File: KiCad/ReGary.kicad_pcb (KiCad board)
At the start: 4 copper layers, 38 x 38 mm, 39 parts, among them J1 Conn_01x02, U1 GW1N-UV1P5LQ100, U2 LM1117-3.3, U3 TPS73643DBV, U4 SN74CBT16210, U5 SN74CBT16210, U6 SN74CBT16210, U7 SN74CBT16210, U8 PLCC_84_plug, U9 PLCC_84_plug

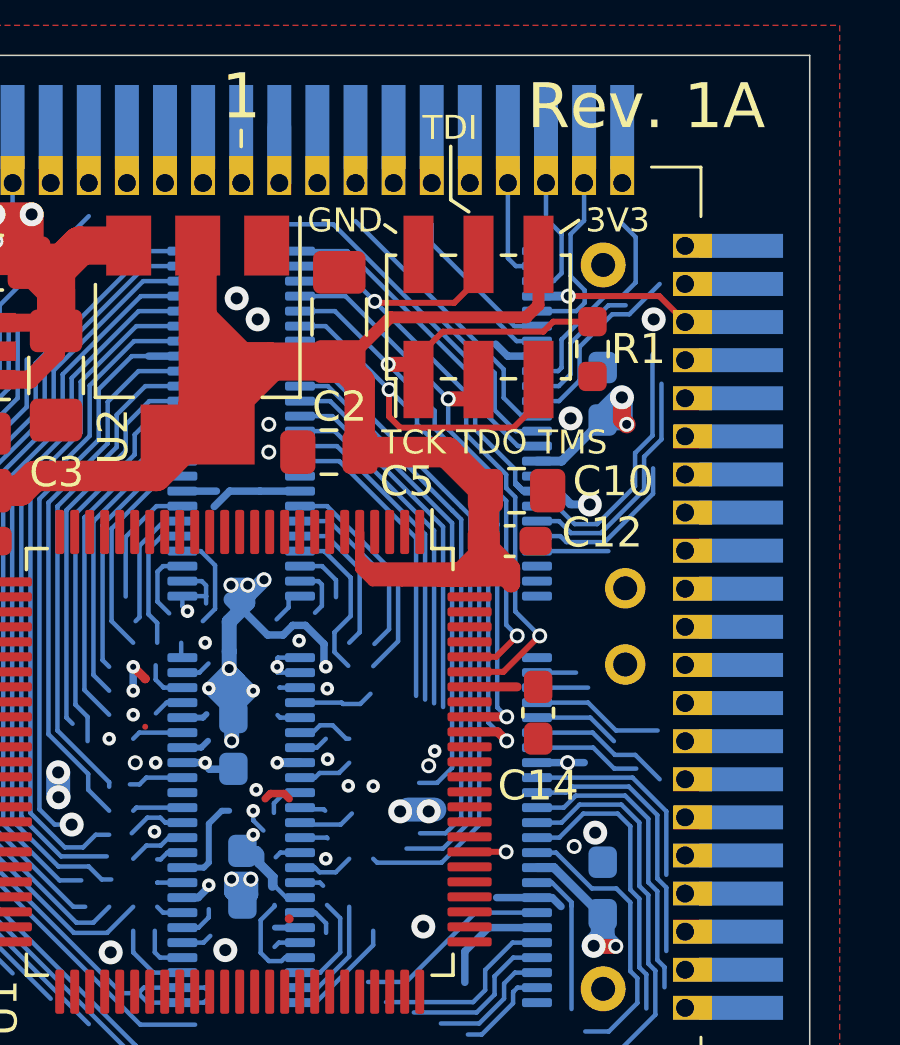
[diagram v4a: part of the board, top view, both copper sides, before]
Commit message: More signal to pin assignments and routing
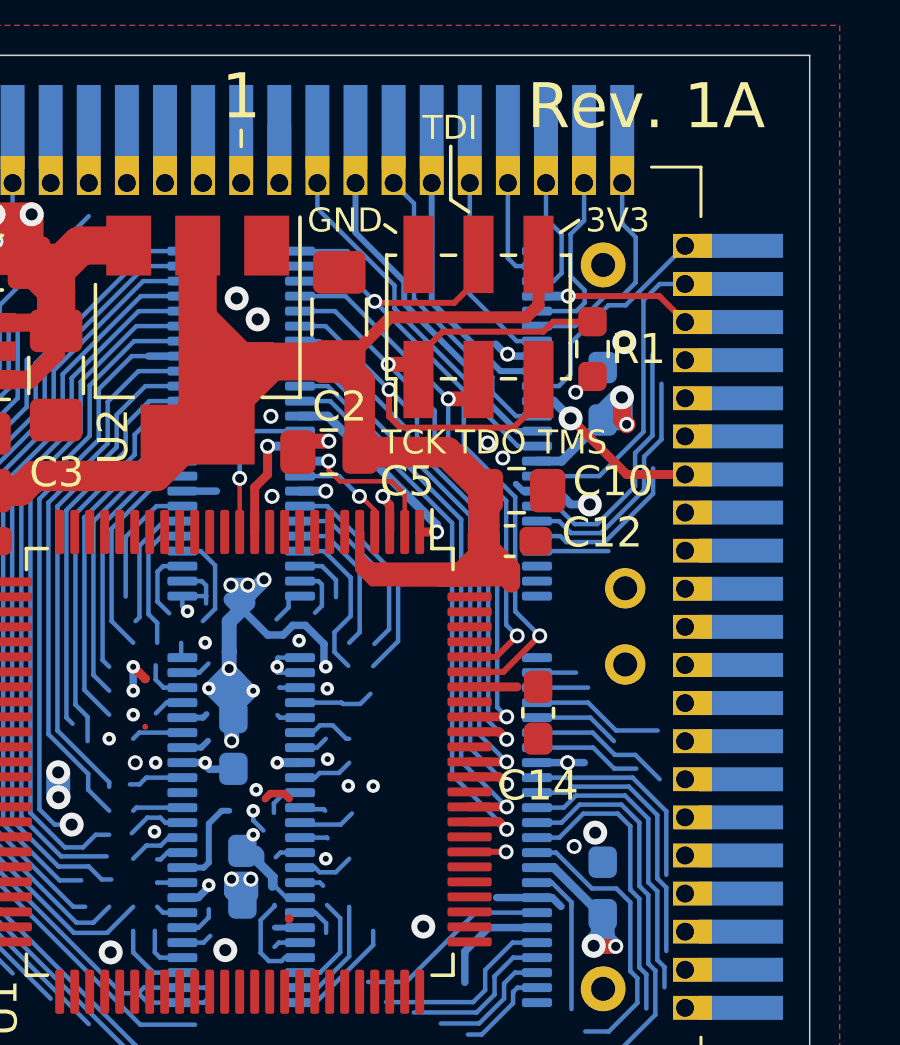
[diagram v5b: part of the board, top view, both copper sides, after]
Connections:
- net Net-(U1-Pad11) renamed /ReGary_FPGA/NC
- net Net-(U1-Pad20) renamed GCLKT_5
- net Net-(U1-Pad3) renamed GCLKT_7
- net Net-(U1-Pad34) renamed GCLKT_4
- net Net-(U1-Pad38) renamed GCLKT_3
- net Net-(U1-Pad63) renamed GCLKT_2
- U1 pad 1: Net-(U1-Pad1) -> C28M_FPGA
- U1 pad 12: Net-(U1-Pad12) -> XCLK_FPGA
- U1 pad 13: Net-(U1-Pad13) -> XCLKEN_FPGA
- U1 pad 2: Net-(U1-Pad2) -> BIGZ_FPGA
- U1 pad 4: Net-(U1-Pad4) -> STERM_FPGA
- U1 pad 84: Net-(U1-Pad84) -> DS_FPGA
- U1 pad 85: Net-(U1-Pad85) -> AGCLK_FPGA
- U1 pad 87: Net-(U1-Pad87) -> UUDS_FPGA
- U1 pad 88: Net-(U1-Pad88) -> C3_FPGA
- U4 pad 10: EBG0 -> DS
- U4 pad 11: EBG1 -> C28M
- U4 pad 12: BINT -> XCLKEN
- U4 pad 13: EDS1 -> XCLK
- U4 pad 14: FCS -> BIGZ
- U4 pad 16: GND -> STERM
- U4 pad 33: Net-(U4-Pad33) -> STERM_FPGA
- U4 pad 34: FCS_FPGA -> BIGZ_FPGA
- U4 pad 35: EDS1_FPGA -> XCLK_FPGA
- U4 pad 36: BINT_FPGA -> XCLKEN_FPGA
- U4 pad 37: EBG1_FPGA -> C28M_FPGA
- U4 pad 38: EBG0_FPGA -> DS_FPGA
- U4 pad 39: ABOE1_FPGA -> AGCLK_FPGA
- U4 pad 40: MS0_FPGA -> UUDS_FPGA
- U4 pad 42: EBR0_FPGA -> C3_FPGA
- U4 pad 6: EBR0 -> C3
- U4 pad 7: MS0 -> UUDS
- U4 pad 9: ABOE1 -> AGCLK
- U8 pad 43: Net-(U8-Pad43) -> CPUCLK
- U8 pad 44: Net-(U8-Pad44) -> KBCLK
- U8 pad 64: Net-(U8-Pad64) -> ECLK
- U8 pad 65: Net-(U8-Pad65) -> C1
- U8 pad 66: Net-(U8-Pad66) -> CDAC
- U8 pad 67: Net-(U8-Pad67) -> C7M
- U8 pad 68: Net-(U8-Pad68) -> C28M
- U8 pad 69: Net-(U8-Pad69) -> TEST
- U8 pad 70: Net-(U8-Pad70) -> CLK90
- U8 pad 71: Net-(U8-Pad71) -> D31
- U8 pad 73: Net-(U8-Pad73) -> STERM
- U8 pad 74: Net-(U8-Pad74) -> DS
- U8 pad 75: Net-(U8-Pad75) -> C3
- U8 pad 80: Net-(U8-Pad80) -> AGCLK
- U8 pad 81: Net-(U8-Pad81) -> XCLKEN
- U8 pad 82: Net-(U8-Pad82) -> XCLK
- U8 pad 83: Net-(U8-Pad83) -> BIGZ
- U9 pad 43: Net-(U9-Pad43) -> CPUCLK
- U9 pad 44: Net-(U9-Pad44) -> KBCLK
- U9 pad 64: Net-(U9-Pad64) -> ECLK
- U9 pad 65: Net-(U9-Pad65) -> C1
- U9 pad 66: Net-(U9-Pad66) -> CDAC
- U9 pad 67: Net-(U9-Pad67) -> C7M
- U9 pad 68: Net-(U9-Pad68) -> C28M
- U9 pad 69: Net-(U9-Pad69) -> TEST
- U9 pad 70: Net-(U9-Pad70) -> CLK90
- U9 pad 71: Net-(U9-Pad71) -> D31
- U9 pad 73: Net-(U9-Pad73) -> STERM
- U9 pad 74: Net-(U9-Pad74) -> DS
- U9 pad 75: Net-(U9-Pad75) -> C3
- U9 pad 80: Net-(U9-Pad80) -> AGCLK
- U9 pad 81: Net-(U9-Pad81) -> XCLKEN
- U9 pad 82: Net-(U9-Pad82) -> XCLK
- U9 pad 83: Net-(U9-Pad83) -> BIGZ
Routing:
- net MS0_FPGA: track 20.4 -> 0.00 mm
- net DS_FPGA: track 25.7 -> 44.8 mm, vias 0 -> 1
- net ABOE1_FPGA: track 18.7 -> 0.00 mm
- net AGCLK_FPGA: track 0.00 -> 18.7 mm, vias 0 -> 1
- net C3_FPGA: track 0.00 -> 18.5 mm, vias 0 -> 1
- net UUDS_FPGA: track 0.00 -> 18.5 mm, vias 0 -> 1
- net EBG0_FPGA: track 16.2 -> 0.00 mm
- net EBR0_FPGA: track 15.4 -> 0.00 mm
- net EBG1_FPGA: track 12.3 -> 0.00 mm
- net FCS: track 12.3 -> 0.00 mm
- net BIGZ: track 2.38 -> 14.6 mm
- net BINT_FPGA: track 11.6 -> 0.00 mm
- net XCLK: track 0.00 -> 11.2 mm
- net EDS1_FPGA: track 10.9 -> 0.00 mm
- net GND: track 124.4 -> 114.0 mm, vias 42 -> 44
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- removed copper zone on 4V3.Cu, net 3V3
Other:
- net class Default: via_dia 0.45 -> 0.5; via_drill 0.2 -> 0.3
- rule via_min_size: 0.45 -> 0.5

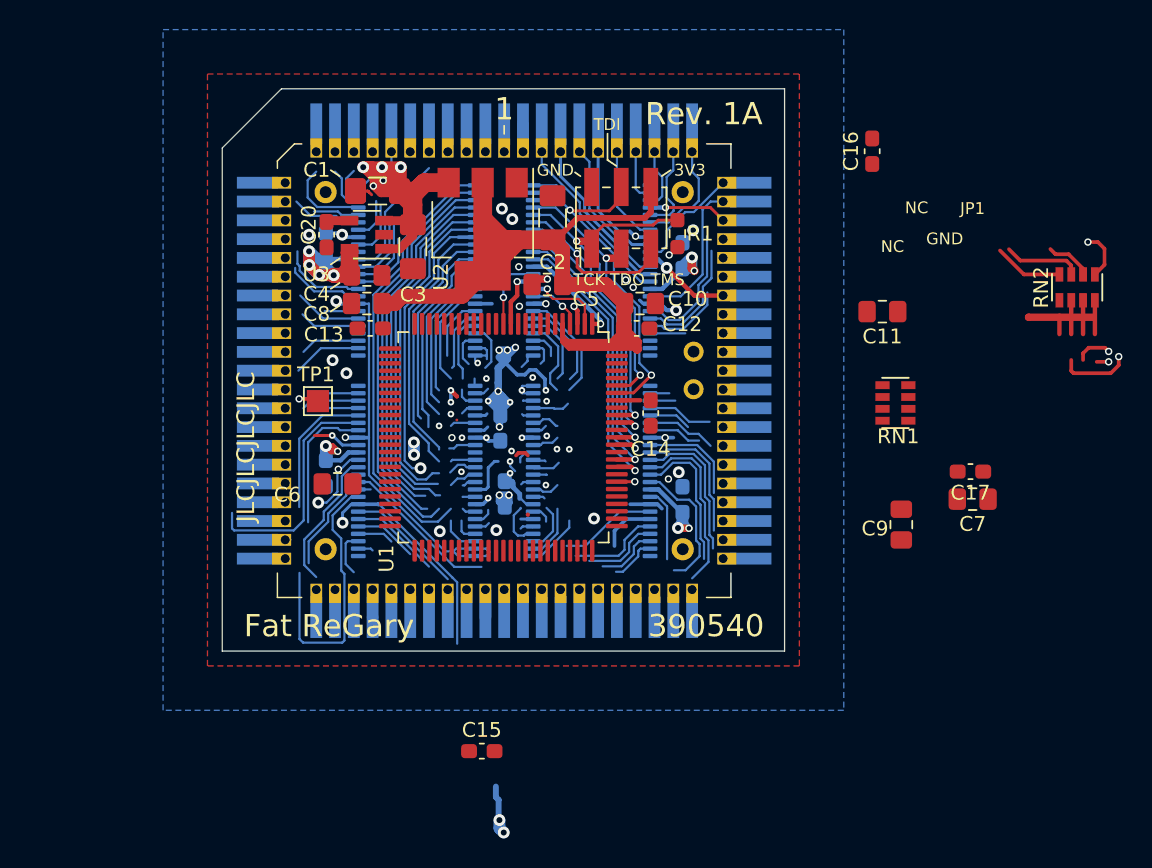
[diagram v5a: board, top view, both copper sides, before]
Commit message: More FPGA pin assignments and routing
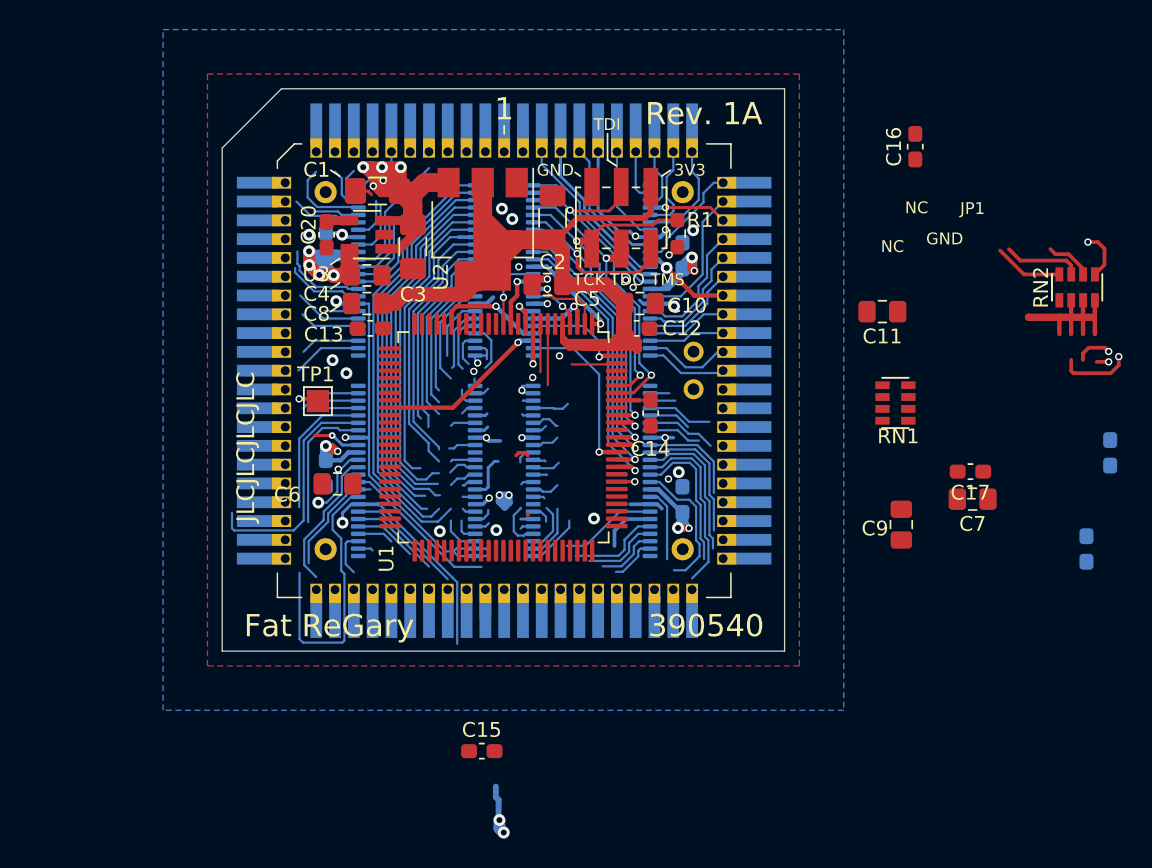
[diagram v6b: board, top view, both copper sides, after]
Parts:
- moved C19 41.2 mm to (185.4, 80.0)
- moved C18 39.5 mm to (183.8, 86.5)
- moved C16 2.93 mm to (172.2, 59.3)
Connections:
- U1 pad 10: Net-(U1-Pad10) -> D31_FPGA
- U1 pad 20: GCLKT_5 -> C7M_FPGA
- U1 pad 3: GCLKT_7 -> CLK90_FPGA
- U1 pad 34: GCLKT_4 -> CDAC_FPGA
- U1 pad 86: Net-(U1-Pad86) -> C1_FPGA
- U1 pad 9: Net-(U1-Pad9) -> ECLK_FPGA
- U1 pad 99: Net-(U1-Pad99) -> TEST_FPGA
- U4 pad 18: EBG2 -> D31
- U4 pad 19: EBG3 -> CLK90
- U4 pad 20: EBG4 -> TEST
- U4 pad 21: BIGZ -> C7M
- U4 pad 22: SLAVE0 -> CDAC
- U4 pad 23: SLAVE1 -> C1
- U4 pad 24: SLAVE2 -> ECLK
- U4 pad 25: SLAVE2_FPGA -> ECLK_FPGA
- U4 pad 26: SLAVE1_FPGA -> C1_FPGA
- U4 pad 27: SLAVE0_FPGA -> CDAC_FPGA
- U4 pad 28: BIGZ_FPGA -> C7M_FPGA
- U4 pad 29: EBG4_FPGA -> TEST_FPGA
- U4 pad 30: EBG3_FPGA -> CLK90_FPGA
- U4 pad 31: EBG2_FPGA -> D31_FPGA
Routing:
- net 3V3: track 121.3 -> 94.3 mm, vias 19 -> 4
- net C1_FPGA: track 0.00 -> 11.6 mm, vias 0 -> 1
- net CDAC_FPGA: track 3.11 -> 14.7 mm, vias 0 -> 1
- net TDO: track 10.3 -> 0.00 mm
- net D31: track 0.00 -> 8.68 mm
- net EBG2: track 8.67 -> 0.00 mm
- net EBG3: track 8.12 -> 0.01 mm
- net CLK90: track 3.76 -> 11.5 mm
- net EBG2_FPGA: track 7.56 -> 0.00 mm, vias 1 -> 0
- net C7M_FPGA: track 0.95 -> 8.20 mm, vias 0 -> 1
- net TEST_FPGA: track 0.00 -> 7.16 mm, vias 0 -> 1
- net GND: track 114.0 -> 106.9 mm, vias 44 -> 35
- net 4V3: track 41.8 -> 48.8 mm
- net TEST: track 0.00 -> 6.76 mm
- net TCK: track 11.4 -> 4.68 mm
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
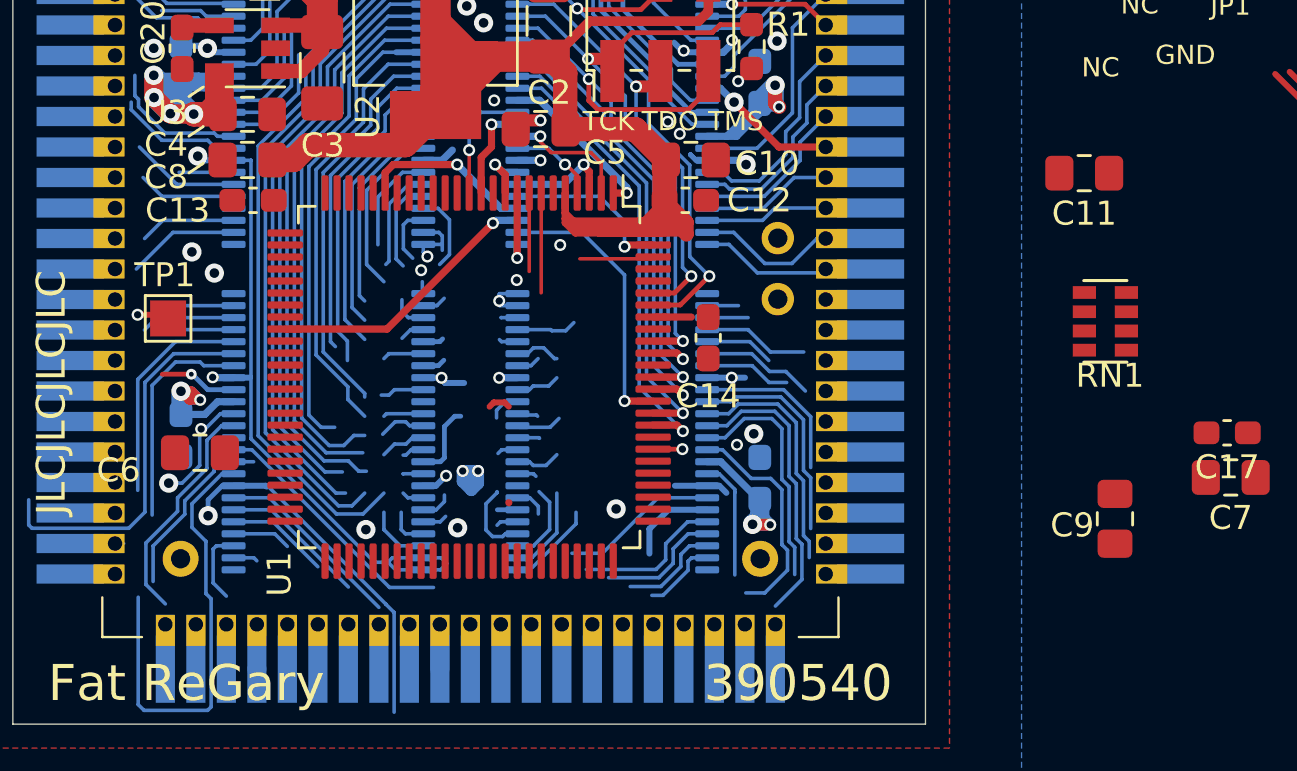
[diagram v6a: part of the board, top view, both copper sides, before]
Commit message: More signal to pin assignments and routing
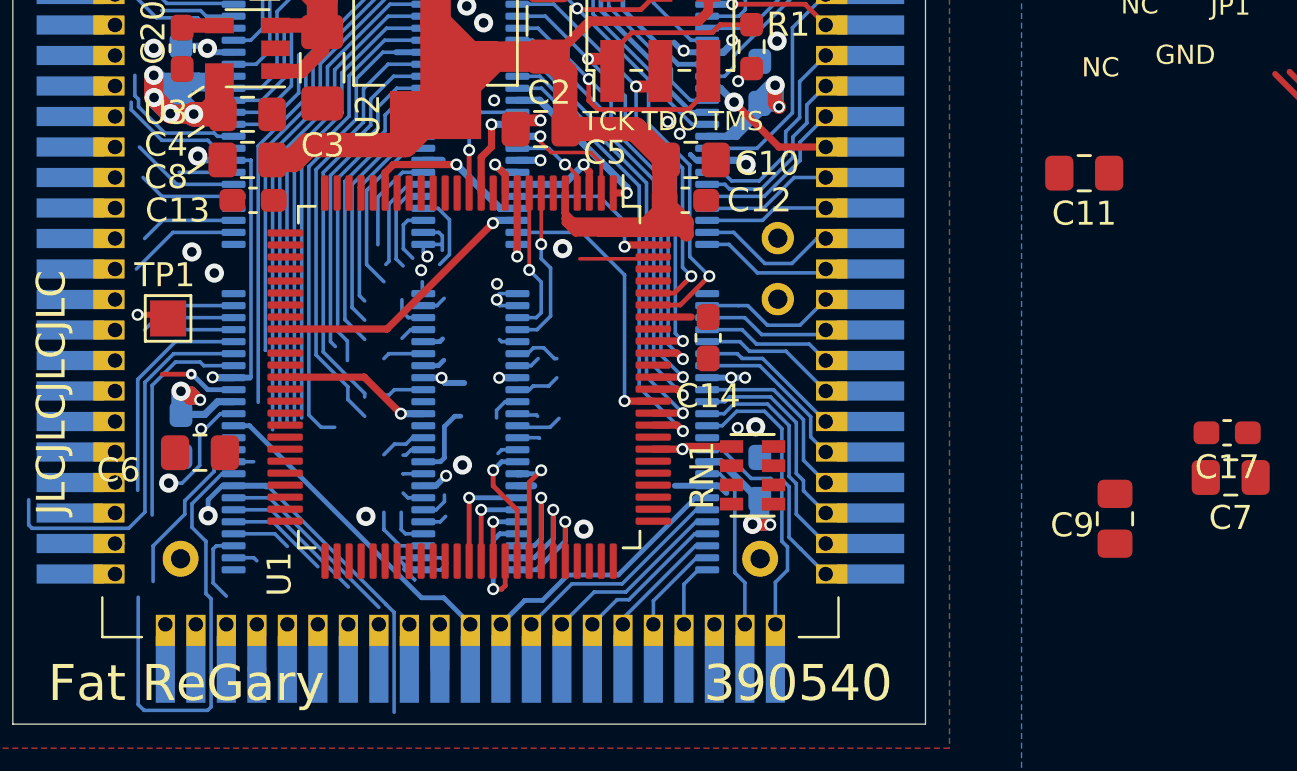
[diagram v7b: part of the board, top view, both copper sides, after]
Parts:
- moved RN1 16.0 mm to (156.2, 83.0)
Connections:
- net EBGACK_FPGA renamed A12_FPGA
- net EDS0_FPGA renamed BLS_FPGA
- net MEMZ2 renamed Net-(U6-Pad13)
- net MEMZ2_FPGA renamed Net-(U6-Pad35)
- net OWN_FPGA renamed PWRUP_FPGA
- U1 pad 38: GCLKT_3 -> CPUCLK_FPGA
- U1 pad 63: GCLKT_2 -> KBCLK_FPGA
- U1 pad 64: Net-(U1-Pad64) -> DMAC_FPGA
- U1 pad 65: Net-(U1-Pad65) -> CIA1_FPGA
- U1 pad 66: Net-(U1-Pad66) -> CIA0_FPGA
- U1 pad 67: Net-(U1-Pad67) -> ROMOE_FPGA
- U1 pad 68: Net-(U1-Pad68) -> RTCRD_FPGA
- U1 pad 69: Net-(U1-Pad69) -> FPU_FPGA
- U1 pad 7: Net-(U1-Pad7) -> REGEN_FPGA
- U1 pad 70: Net-(U1-Pad70) -> SLOT_FPGA
- U1 pad 71: Net-(U1-Pad71) -> RTCWR_FPGA
- U1 pad 74: Net-(U1-Pad74) -> OECD_FPGA
- U1 pad 75: Net-(U1-Pad75) -> LCD_FPGA
- U1 pad 76: Net-(U1-Pad76) -> UDS_FPGA
- U1 pad 77: Net-(U1-Pad77) -> LDS_FPGA
- U1 pad 78: Net-(U1-Pad78) -> DBR_FPGA
- U1 pad 8: Net-(U1-Pad8) -> RAMEN_FPGA
- U6 pad 10: OWN -> PWRUP
- U6 pad 11: MS1 -> LCD
- U6 pad 12: ADDRZ3 -> OECD
- U6 pad 14: IOZ2 -> ROMOE
- U6 pad 16: CBACK -> RTCRD
- U6 pad 18: ABOE0 -> KBCLK
- U6 pad 19: CLK90 -> DMAC
- U6 pad 2: SLAVE3 -> RAMEN
- U6 pad 20: MS2 -> CIA1
- U6 pad 21: MTCR -> CIA0
- U6 pad 22: CINH -> FPU
- U6 pad 23: A3 -> SLOT
- U6 pad 24: CBREQ -> RTCWR
- U6 pad 25: CBREQ_FPGA -> RTCWR_FPGA
- U6 pad 26: A3_FPGA -> SLOT_FPGA
- U6 pad 27: CINH_FPGA -> FPU_FPGA
- U6 pad 28: MTCR_FPGA -> CIA0_FPGA
- U6 pad 29: MS2_FPGA -> CIA1_FPGA
- U6 pad 3: EBCLR -> REGEN
- U6 pad 30: CLK90_FPGA -> DMAC_FPGA
- U6 pad 31: ABOE0_FPGA -> KBCLK_FPGA
- U6 pad 33: CBACK_FPGA -> RTCRD_FPGA
- U6 pad 34: IOZ2_FPGA -> ROMOE_FPGA
- U6 pad 36: ADDRZ3_FPGA -> OECD_FPGA
- U6 pad 37: MS1_FPGA -> LCD_FPGA
- U6 pad 4: EDS0 -> BLS
- U6 pad 40: SLAVE4_FPGA -> UDS_FPGA
- U6 pad 42: EA2_FPGA -> LDS_FPGA
- U6 pad 43: EA3_FPGA -> DBR_FPGA
- U6 pad 45: EBCLR_FPGA -> REGEN_FPGA
- U6 pad 46: SLAVE3_FPGA -> RAMEN_FPGA
- U6 pad 5: EA3 -> DBR
- U6 pad 6: EA2 -> LDS
- U6 pad 7: SLAVE4 -> UDS
- U6 pad 9: EBGACK -> A12
- U7 pad 13: D2P -> CPUCLK
- U7 pad 29: CPUCLK_FPGA -> Net-(U7-Pad29)
- U7 pad 35: D2P_FPGA -> CPUCLK_FPGA
- U8 pad 45: Net-(U8-Pad45) -> DMAC
- U8 pad 46: Net-(U8-Pad46) -> CIA1
- U8 pad 47: Net-(U8-Pad47) -> CIA0
- U8 pad 48: Net-(U8-Pad48) -> FPU
- U8 pad 49: Net-(U8-Pad49) -> SLOT
- U8 pad 50: Net-(U8-Pad50) -> RTCWR
- U8 pad 52: Net-(U8-Pad52) -> RTCRD
- U8 pad 53: Net-(U8-Pad53) -> ROMOE
- U8 pad 54: Net-(U8-Pad54) -> OECD
- U8 pad 55: Net-(U8-Pad55) -> LCD
- U8 pad 56: Net-(U8-Pad56) -> PWRUP
- U8 pad 57: Net-(U8-Pad57) -> A12
- U8 pad 58: Net-(U8-Pad58) -> UDS
- U8 pad 59: Net-(U8-Pad59) -> LDS
- U8 pad 60: Net-(U8-Pad60) -> DBR
- U8 pad 61: Net-(U8-Pad61) -> BLS
- U8 pad 62: Net-(U8-Pad62) -> REGEN
- U8 pad 63: Net-(U8-Pad63) -> RAMEN
- U9 pad 45: Net-(U9-Pad45) -> DMAC
- U9 pad 46: Net-(U9-Pad46) -> CIA1
- U9 pad 47: Net-(U9-Pad47) -> CIA0
- U9 pad 48: Net-(U9-Pad48) -> FPU
- U9 pad 49: Net-(U9-Pad49) -> SLOT
- U9 pad 50: Net-(U9-Pad50) -> RTCWR
- U9 pad 52: Net-(U9-Pad52) -> RTCRD
- U9 pad 53: Net-(U9-Pad53) -> ROMOE
- U9 pad 54: Net-(U9-Pad54) -> OECD
- U9 pad 55: Net-(U9-Pad55) -> LCD
- U9 pad 56: Net-(U9-Pad56) -> PWRUP
- U9 pad 57: Net-(U9-Pad57) -> A12
- U9 pad 58: Net-(U9-Pad58) -> UDS
- U9 pad 59: Net-(U9-Pad59) -> LDS
- U9 pad 60: Net-(U9-Pad60) -> DBR
- U9 pad 61: Net-(U9-Pad61) -> BLS
- U9 pad 62: Net-(U9-Pad62) -> REGEN
- U9 pad 63: Net-(U9-Pad63) -> RAMEN
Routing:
- net CPUCLK: track 9.26 -> 22.5 mm
- net ADDRZ3: track 12.1 -> 0.00 mm
- net GND: track 106.9 -> 95.5 mm, vias 35 -> 36
- net KBCLK: track 0.00 -> 10.8 mm
- net ABOE2: track 10.7 -> 0.00 mm
- net OECD: track 0.00 -> 10.5 mm
- net MS1: track 10.0 -> 0.00 mm
- net Net-(U6-Pad13): track 9.91 -> 0.00 mm
- net ROMOE: track 0.00 -> 9.71 mm
- net D2P: track 9.56 -> 0.00 mm
- net LCD: track 0.00 -> 9.49 mm
- net IOZ2: track 9.38 -> 0.00 mm
- net DMAC: track 0.00 -> 9.30 mm
- net OWN: track 9.14 -> 0.00 mm
- net AS_FPGA: track 27.9 -> 18.9 mm
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
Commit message: Placement of caps and more routing
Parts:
- removed RN2: 10k, ReGary:RESCAF80P320X160X60-8N
- moved C11 22.6 mm to (154.4, 86.8), turned to 90 degrees
- moved C15 16.3 mm to (152.7, 87.1), turned to 90 degrees
- moved C9 16.2 mm to (156.2, 78.9), turned to 90 degrees
- moved C17 4.14 mm to (174.8, 77.3)
- moved C14 0.30 mm to (154.5, 77.1)
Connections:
- RN1 pad 2: Net-(RN1-Pad2) -> RECONFIG_N
- RN1 pad 3: Net-(RN1-Pad3) -> LDS_FPGA
- RN1 pad 4: Net-(RN1-Pad4) -> UDS_FPGA
- U6 pad 13: Net-(U6-Pad13) -> GND
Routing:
- net 3V3: track 91.4 -> 156.4 mm
- net GND: track 95.5 -> 103.4 mm, vias 36 -> 37
- net OECD_FPGA: track 0.93 -> 8.46 mm
- net LCD_FPGA: track 1.91 -> 8.84 mm, vias 0 -> 1
- net LDS_FPGA: track 0.98 -> 6.16 mm, vias 0 -> 1
- net RECONFIG_N: track 0.00 -> 3.34 mm
- net 4V3: track 48.8 -> 50.7 mm
- net UDS_FPGA: track 1.85 -> 3.22 mm, vias 0 -> 1
- net DBR_FPGA: track 1.93 -> 3.04 mm, vias 0 -> 1
